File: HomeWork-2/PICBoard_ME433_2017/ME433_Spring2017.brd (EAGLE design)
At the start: 50 x 50 mm, 21 parts, among them J1 USB-MB-H

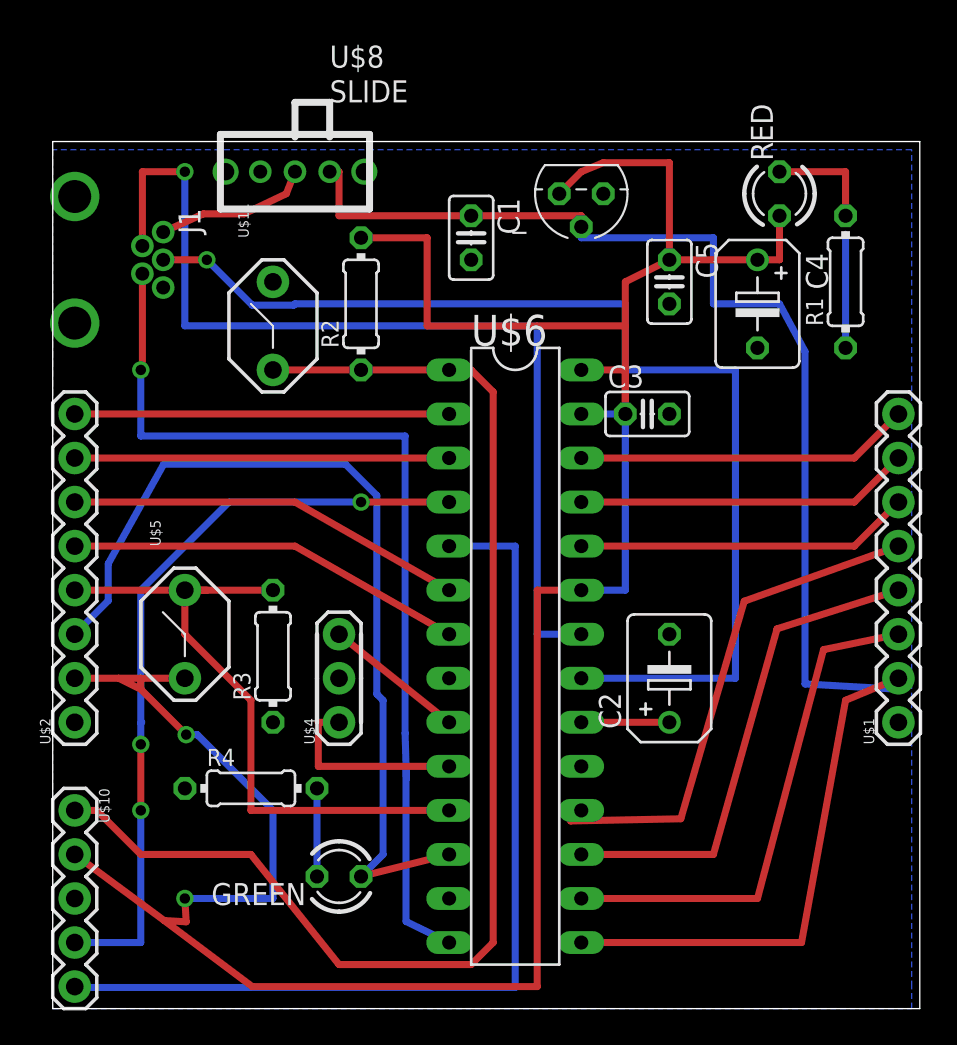
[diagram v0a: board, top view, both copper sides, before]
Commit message: Final Layout draft#2: Parse error for DRC
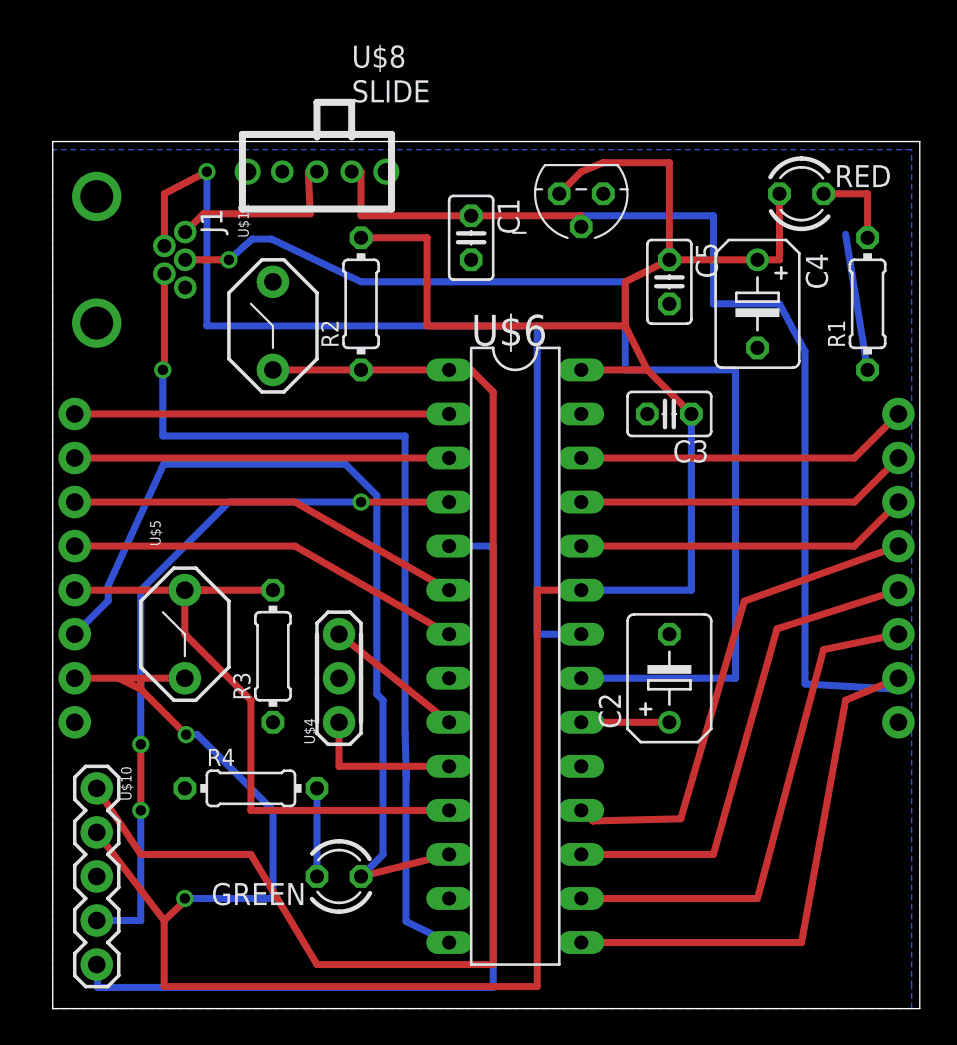
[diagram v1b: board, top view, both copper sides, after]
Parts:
- U$2: value BRANCHOUT_2 -> BRANCHOUT_1
- moved U$10 1.80 mm to (2.54, 12.7)
- moved R1 1.80 mm to (47.0, 40.6)
- moved C3 1.27 mm to (35.6, 34.3), turned to 180 degrees
- moved RED 1.27 mm to (43.2, 47.0), turned to 0 degrees
- moved J1 1.27 mm to (2.54, 43.2)
- moved U$8 1.27 mm to (15.2, 48.3)
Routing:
- net +3V3: track 157.7 -> 163.2 mm
- net PGC: track 54.7 -> 52.1 mm
- net PGD: track 44.0 -> 41.5 mm
- net O1/A3: track 11.3 -> 8.89 mm
- net D-: track 56.3 -> 54.0 mm
- net N$1: track 8.95 -> 10.6 mm
- net GND: track 6.55 -> 7.93 mm
- net N$18: track 6.35 -> 5.08 mm
- net ID: track 56.2 -> 54.9 mm
- net B9: track 29.7 -> 28.5 mm
- net MCLR~: track 73.7 -> 74.7 mm
